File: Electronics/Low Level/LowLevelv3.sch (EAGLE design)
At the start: 69 parts, among them IC1_2515 MCP2515, IC2_2551 MCP2551DIL08, IC3_4802 MCP4802, Q1 16MHz, T1 2N3904, T2 2N3904, X1 284512-4, X3 Motor, X4 CLICK

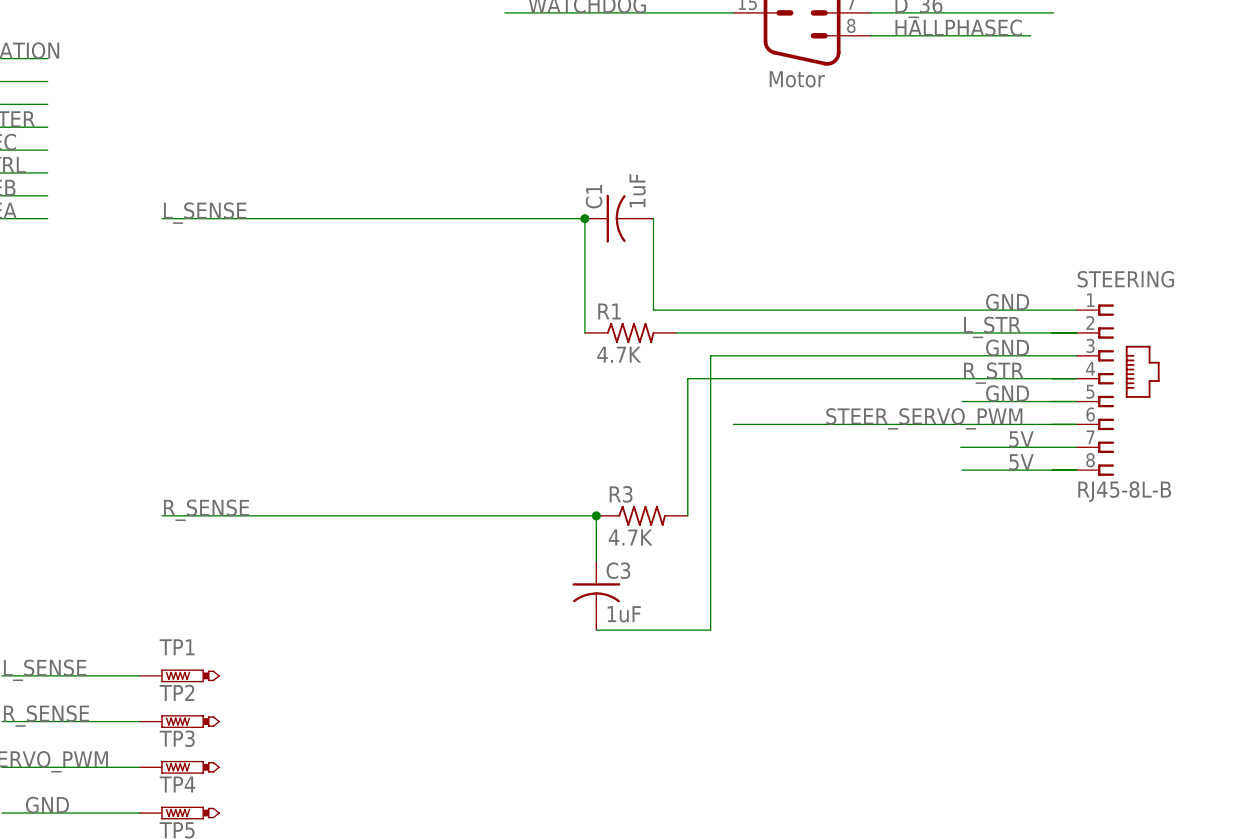
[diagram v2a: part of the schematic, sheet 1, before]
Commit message: Corrections to silkscreen, added testpoints
Fixed silkscreen errors around the relay terminals, added symbols.
Added testpoints and easily cut traces for steering header ground pins, for future expandability options.
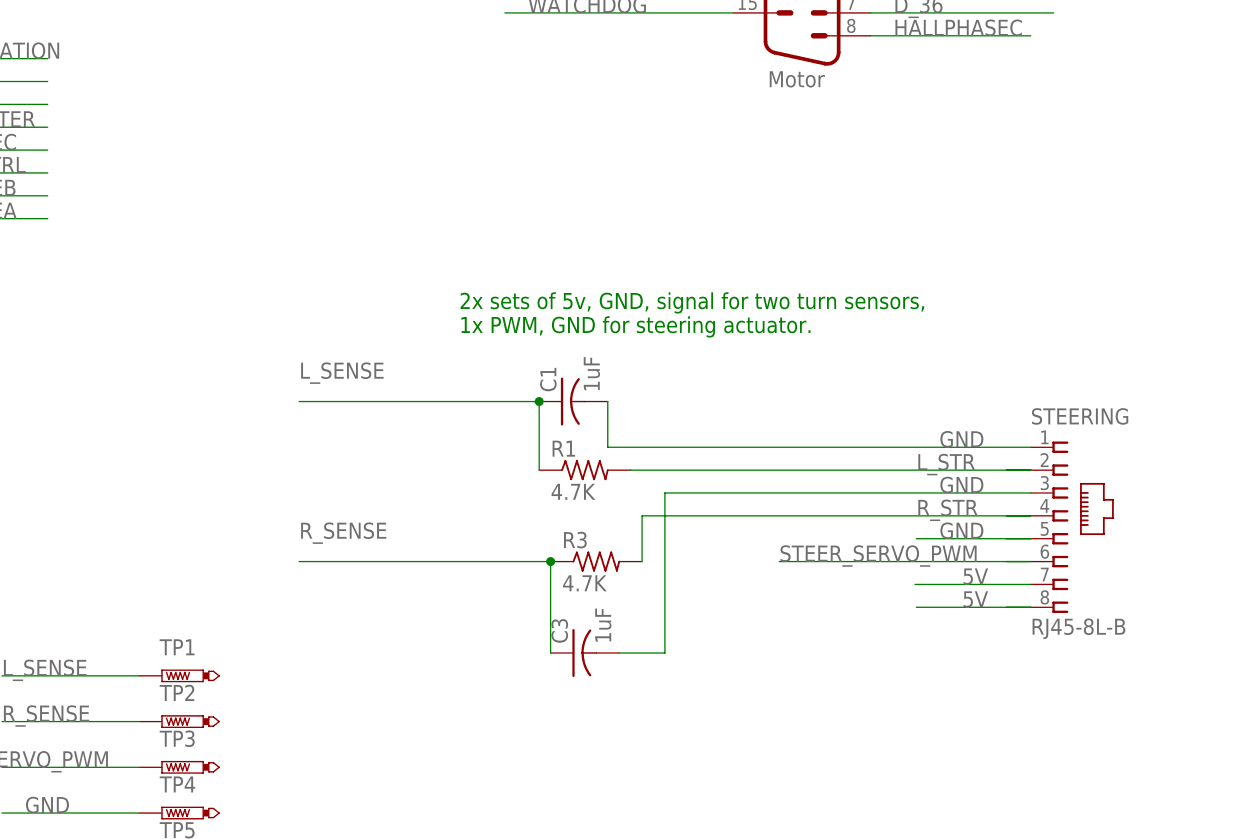
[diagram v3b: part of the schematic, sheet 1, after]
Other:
- note added: "2x sets of 5v, GND, signal for two turn sensors, 1x PWM, GND for steering actuator."
- moved on the sheet: C1, C3, R1, R3, STEERING
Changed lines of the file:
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@@
 <part name="CAN_HEADER" library="SparkFun-Connectors" library_urn="urn:adsk.eagle:library:513" deviceset="CONN_03" device="-SCREW-5MM" package3d_urn="urn:adsk.eagle:package:38070/1"/>
 <part name="R10" library="resistor" library_urn="urn:adsk.eagle:library:348" deviceset="R-US_" device="R1206" package3d_urn="urn:adsk.eagle:package:23540/2" value="120"/>
-<part name="CONNECTORS" library="frames" library_urn="urn:adsk.eagle:library:229" deviceset="A4L-LOC" device=""/>
+<part name="CONNECTORS" library="frames" library_urn="urn:adsk.eagle:library:229" deviceset="A4L-LOC" device="" value="Ports and Pins"/>
 <part name="FRAME1" library="frames" library_urn="urn:adsk.eagle:library:229" deviceset="A4L-LOC" device=""/>
 <part name="FRAME2" library="frames" library_urn="urn:adsk.eagle:library:229" deviceset="A4L-LOC" device=""/>
@@
 <text x="59.69" y="50.419" size="1.778" layer="91">GND</text>
 <text x="59.69" y="47.879" size="1.778" layer="91">AREF</text>
+<text x="172.72" y="66.04" size="1.778" layer="91">2x sets of 5v, GND, signal for two turn sensors,
+1x PWM, GND for steering actuator.</text>
 </plain>
 <instances>
@@
 <attribute name="NAME" x="207.01" y="120.65" size="1.778" layer="95"/>
 </instance>
-<instance part="R1" gate="G$1" x="191.77" y="66.04" smashed="yes">
-<attribute name="NAME" x="187.96" y="67.5386" size="1.778" layer="95"/>
-<attribute name="VALUE" x="187.96" y="62.738" size="1.778" layer="96"/>
-</instance>
-<instance part="R3" gate="G$1" x="193.04" y="45.72" smashed="yes">
-<attribute name="NAME" x="189.23" y="47.2186" size="1.778" layer="95"/>
-<attribute name="VALUE" x="189.23" y="42.418" size="1.778" layer="96"/>
-</instance>
-<instance part="C3" gate="G$1" x="187.96" y="38.1" smashed="yes">
-<attribute name="NAME" x="188.976" y="38.735" size="1.778" layer="95"/>
-<attribute name="VALUE" x="188.976" y="33.909" size="1.778" layer="96"/>
-</instance>
-<instance part="C1" gate="G$1" x="189.23" y="78.74" smashed="yes" rot="R90">
-<attribute name="NAME" x="188.595" y="79.756" size="1.778" layer="95" rot="R90"/>
-<attribute name="VALUE" x="193.421" y="79.756" size="1.778" layer="96" rot="R90"/>
+<instance part="R1" gate="G$1" x="186.69" y="50.8" smashed="yes">
+<attribute name="NAME" x="182.88" y="52.2986" size="1.778" layer="95"/>
+<attribute name="VALUE" x="182.88" y="47.498" size="1.778" layer="96"/>
+</instance>
+<instance part="R3" gate="G$1" x="187.96" y="40.64" smashed="yes">
+<attribute name="NAME" x="184.15" y="42.1386" size="1.778" layer="95"/>
+<attribute name="VALUE" x="184.15" y="37.338" size="1.778" layer="96"/>
+</instance>
+<instance part="C3" gate="G$1" x="185.42" y="30.48" smashed="yes" rot="R90">
+<attribute name="NAME" x="184.785" y="31.496" size="1.778" layer="95" rot="R90"/>
+<attribute name="VALUE" x="189.611" y="31.496" size="1.778" layer="96" rot="R90"/>
+</instance>
+<instance part="C1" gate="G$1" x="184.15" y="58.42" smashed="yes" rot="R90">
+<attribute name="NAME" x="183.515" y="59.436" size="1.778" layer="95" rot="R90"/>
+<attribute name="VALUE" x="188.341" y="59.436" size="1.778" layer="96" rot="R90"/>
 </instance>
 <instance part="DIGITAL_8-13" gate="A" x="55.88" y="55.88" smashed="yes">
@@
 <attribute name="SHEET" x="230.505" y="5.08" size="2.54" layer="94"/>
 </instance>
-<instance part="STEERING" gate="G$1" x="243.84" y="60.96" smashed="yes">
-<attribute name="NAME" x="241.3" y="71.12" size="1.778" layer="95"/>
-<attribute name="VALUE" x="241.3" y="47.752" size="1.778" layer="96"/>
+<instance part="STEERING" gate="G$1" x="238.76" y="45.72" smashed="yes">
+<attribute name="NAME" x="236.22" y="55.88" size="1.778" layer="95"/>
+<attribute name="VALUE" x="236.22" y="32.512" size="1.778" layer="96"/>
 </instance>
 <instance part="TP1" gate="G$1" x="139.7" y="27.94" smashed="yes" rot="R90">
@@
 <net name="5V" class="1">
 <segment>
-<label x="233.68" y="53.34" size="1.778" layer="95"/>
-<wire x1="241.3" y1="53.34" x2="228.4476" y2="53.34" width="0.1524" layer="91"/>
+<label x="228.6" y="38.1" size="1.778" layer="95"/>
+<wire x1="236.22" y1="38.1" x2="223.3676" y2="38.1" width="0.1524" layer="91"/>
 <pinref part="STEERING" gate="G$1" pin="7"/>
 </segment>
@@
 </segment>
 <segment>
-<label x="233.68" y="50.8" size="1.778" layer="95"/>
-<wire x1="228.6" y1="50.8" x2="241.3" y2="50.8" width="0.1524" layer="91"/>
+<label x="228.6" y="35.56" size="1.778" layer="95"/>
+<wire x1="223.52" y1="35.56" x2="236.22" y2="35.56" width="0.1524" layer="91"/>
 <pinref part="STEERING" gate="G$1" pin="8"/>
-<wire x1="241.3" y1="50.8" x2="238.6076" y2="50.8" width="0.1524" layer="91"/>
+<wire x1="236.22" y1="35.56" x2="233.5276" y2="35.56" width="0.1524" layer="91"/>
 </segment>
 <segment>
@@
 <segment>
 <pinref part="C3" gate="G$1" pin="2"/>
-<wire x1="187.96" y1="33.02" x2="200.66" y2="33.02" width="0.1524" layer="91"/>
-<label x="231.14" y="63.5" size="1.778" layer="95"/>
-<wire x1="200.66" y1="33.02" x2="200.66" y2="63.5" width="0.1524" layer="91"/>
-<wire x1="200.66" y1="63.5" x2="241.3" y2="63.5" width="0.1524" layer="91"/>
+<wire x1="190.5" y1="30.48" x2="195.58" y2="30.48" width="0.1524" layer="91"/>
+<label x="226.06" y="48.26" size="1.778" layer="95"/>
+<wire x1="195.58" y1="30.48" x2="195.58" y2="48.26" width="0.1524" layer="91"/>
+<wire x1="195.58" y1="48.26" x2="236.22" y2="48.26" width="0.1524" layer="91"/>
 <pinref part="STEERING" gate="G$1" pin="3"/>
 </segment>
@@
 </segment>
 <segment>
-<label x="231.14" y="58.42" size="1.778" layer="95"/>
-<wire x1="238.6076" y1="58.42" x2="241.3" y2="58.42" width="0.1524" layer="91"/>
+<label x="226.06" y="43.18" size="1.778" layer="95"/>
+<wire x1="233.5276" y1="43.18" x2="236.22" y2="43.18" width="0.1524" layer="91"/>
 <pinref part="STEERING" gate="G$1" pin="5"/>
-<wire x1="241.3" y1="58.42" x2="228.6" y2="58.42" width="0.1524" layer="91"/>
+<wire x1="236.22" y1="43.18" x2="223.52" y2="43.18" width="0.1524" layer="91"/>
 </segment>
 <segment>
@@
 <segment>
 <pinref part="C1" gate="G$1" pin="2"/>
-<label x="231.14" y="68.58" size="1.778" layer="95"/>
-<wire x1="194.31" y1="78.74" x2="194.31" y2="68.58" width="0.1524" layer="91"/>
-<wire x1="194.31" y1="68.58" x2="241.3" y2="68.58" width="0.1524" layer="91"/>
+<label x="226.06" y="53.34" size="1.778" layer="95"/>
+<wire x1="189.23" y1="58.42" x2="189.23" y2="53.34" width="0.1524" layer="91"/>
+<wire x1="189.23" y1="53.34" x2="236.22" y2="53.34" width="0.1524" layer="91"/>
 <pinref part="STEERING" gate="G$1" pin="1"/>
 </segment>
@@
 <segment>
 <pinref part="R3" gate="G$1" pin="2"/>
-<wire x1="198.12" y1="45.72" x2="198.12" y2="60.96" width="0.1524" layer="91"/>
-<label x="228.6" y="60.96" size="1.778" layer="95"/>
-<wire x1="198.12" y1="60.96" x2="241.3" y2="60.96" width="0.1524" layer="91"/>
+<wire x1="193.04" y1="40.64" x2="193.04" y2="45.72" width="0.1524" layer="91"/>
+<label x="223.52" y="45.72" size="1.778" layer="95"/>
+<wire x1="193.04" y1="45.72" x2="236.22" y2="45.72" width="0.1524" layer="91"/>
 <pinref part="STEERING" gate="G$1" pin="4"/>
-<wire x1="241.3" y1="60.96" x2="238.6076" y2="60.96" width="0.1524" layer="91"/>
+<wire x1="236.22" y1="45.72" x2="233.5276" y2="45.72" width="0.1524" layer="91"/>
 </segment>
 </net>
@@
 <segment>
 <pinref part="R1" gate="G$1" pin="2"/>
-<label x="228.6" y="66.04" size="1.778" layer="95"/>
-<wire x1="196.85" y1="66.04" x2="241.3" y2="66.04" width="0.1524" layer="91"/>
+<label x="223.52" y="50.8" size="1.778" layer="95"/>
+<wire x1="191.77" y1="50.8" x2="236.22" y2="50.8" width="0.1524" layer="91"/>
 <pinref part="STEERING" gate="G$1" pin="2"/>
-<wire x1="241.3" y1="66.04" x2="238.6076" y2="66.04" width="0.1524" layer="91"/>
+<wire x1="236.22" y1="50.8" x2="233.5276" y2="50.8" width="0.1524" layer="91"/>
 </segment>
 </net>
@@
 </segment>
 <segment>
-<label x="213.36" y="55.88" size="1.778" layer="95"/>
-<wire x1="238.6076" y1="55.88" x2="241.3" y2="55.88" width="0.1524" layer="91"/>
+<label x="208.28" y="40.64" size="1.778" layer="95"/>
+<wire x1="233.5276" y1="40.64" x2="236.22" y2="40.64" width="0.1524" layer="91"/>
 <pinref part="STEERING" gate="G$1" pin="6"/>
-<wire x1="241.3" y1="55.88" x2="203.2" y2="55.88" width="0.1524" layer="91"/>
+<wire x1="236.22" y1="40.64" x2="208.28" y2="40.64" width="0.1524" layer="91"/>
 </segment>
 <segment>
@@
 <pinref part="C3" gate="G$1" pin="1"/>
 <pinref part="R3" gate="G$1" pin="1"/>
-<wire x1="187.96" y1="45.72" x2="187.96" y2="40.64" width="0.1524" layer="91"/>
-<label x="139.7" y="45.72" size="1.778" layer="95"/>
-<junction x="187.96" y="45.72"/>
-<wire x1="187.96" y1="45.72" x2="139.7" y2="45.72" width="0.1524" layer="91"/>
+<wire x1="182.88" y1="40.64" x2="182.88" y2="30.48" width="0.1524" layer="91"/>
+<label x="154.94" y="43.18" size="1.778" layer="95"/>
+<junction x="182.88" y="40.64"/>
+<wire x1="182.88" y1="40.64" x2="154.94" y2="40.64" width="0.1524" layer="91"/>
 </segment>
 <segment>
@@
 <segment>
 <pinref part="R1" gate="G$1" pin="1"/>
-<label x="139.7" y="78.74" size="1.778" layer="95"/>
+<label x="154.94" y="60.96" size="1.778" layer="95"/>
 <pinref part="C1" gate="G$1" pin="1"/>
-<wire x1="186.69" y1="78.74" x2="186.69" y2="66.04" width="0.1524" layer="91"/>
-<wire x1="186.69" y1="78.74" x2="139.7" y2="78.74" width="0.1524" layer="91"/>
-<junction x="186.69" y="78.74"/>
+<wire x1="181.61" y1="58.42" x2="181.61" y2="50.8" width="0.1524" layer="91"/>
+<wire x1="181.61" y1="58.42" x2="154.94" y2="58.42" width="0.1524" layer="91"/>
+<junction x="181.61" y="58.42"/>
 </segment>
 <segment>
@@
 </drawing>
 <compatibility>
+<note version="6.3" minversion="6.2.2" severity="warning">
+Since Version 6.2.2 text objects can contain more than one line,
+which will not be processed correctly with this version.
+</note>
 <note version="8.2" severity="warning">
 Since Version 8.2, EAGLE supports online libraries. The ids
